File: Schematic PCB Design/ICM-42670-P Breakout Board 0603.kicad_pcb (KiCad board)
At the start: 2 copper layers, 19.5 x 26.5 mm, 14 parts, among them J2 Conn_01x09_Pin, U1 ICM-42670-P, U3 MCP1700x-330xxTT

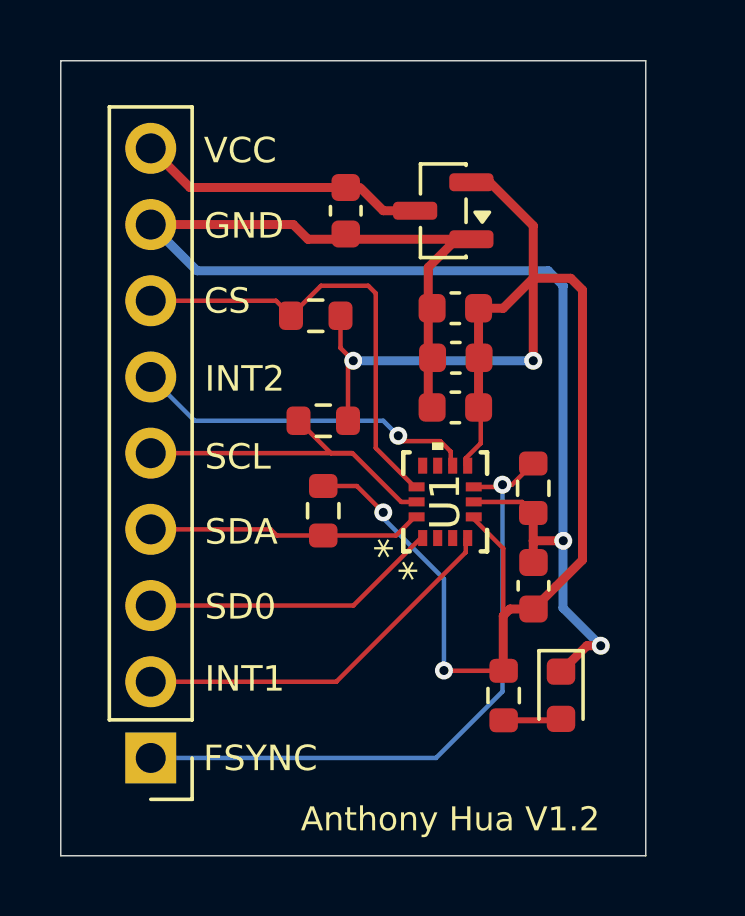
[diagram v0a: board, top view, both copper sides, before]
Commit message: Rerouted Traces and Added Ground Plane
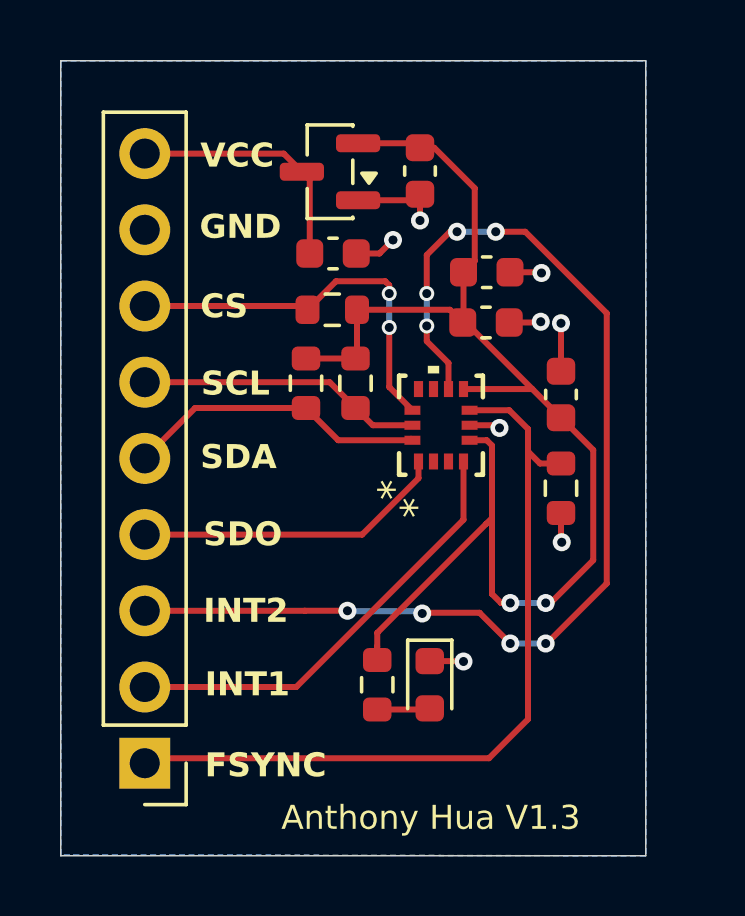
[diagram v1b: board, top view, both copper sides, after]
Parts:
- moved C3 6.44 mm to (72.2, 34.1)
- moved C4 4.72 mm to (67.5, 26.7), turned to 90 degrees
- moved C2 4.63 mm to (69.7, 30.1), turned to 0 degrees
- moved D1 4.39 mm to (67.8, 43.8)
- moved R5 4.29 mm to (63.7, 33.8)
- moved R3 4.23 mm to (66.0, 43.8)
- moved U3 3.99 mm to (64.5, 26.7)
- moved U1 2.56 mm to (68.2, 35.1)
- moved R4 1.65 mm to (65.3, 33.8), turned to 90 degrees
- moved C1 1.55 mm to (69.7, 31.7), turned to 0 degrees
- moved C5 1.49 mm to (64.6, 29.4), turned to 180 degrees
- moved R2 0.92 mm to (72.2, 37.2)
- moved R1 0.59 mm to (64.5, 31.3)
- moved J2 0.27 mm to (58.3, 46.4)
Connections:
- J2 pad 3: /SDO -> /INT2
- J2 pad 4: /SDA -> /SDO
- J2 pad 5: /SCL -> /SDA
- J2 pad 6: /INT2 -> /SCL
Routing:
- net GND: track 50.0 -> 11.0 mm, vias 2 -> 8
- net /INT2: track 11.5 -> 38.0 mm, vias 1 -> 8
- net /3V3_Clean: track 55.7 -> 44.3 mm, vias 4 -> 2
- net /FSYNC: track 22.0 -> 26.5 mm, vias 1 -> 0
- net /CS: track 15.2 -> 13.0 mm, vias 0 -> 2
- net /SCL: track 11.7 -> 9.52 mm
- net /INT1: track 12.8 -> 14.9 mm
- net /SDA: track 9.14 -> 10.1 mm
- net /5V / 3V3: track 9.20 -> 8.32 mm
- net /SDO: track 9.93 -> 10.5 mm
- added copper zone on B.Cu, net GND
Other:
- board text added: "Anthony Hua V1.3"
- board text added: "SDO"
- board text removed: "Anthony Hua V1.2"

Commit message: Add Mounting holes M2
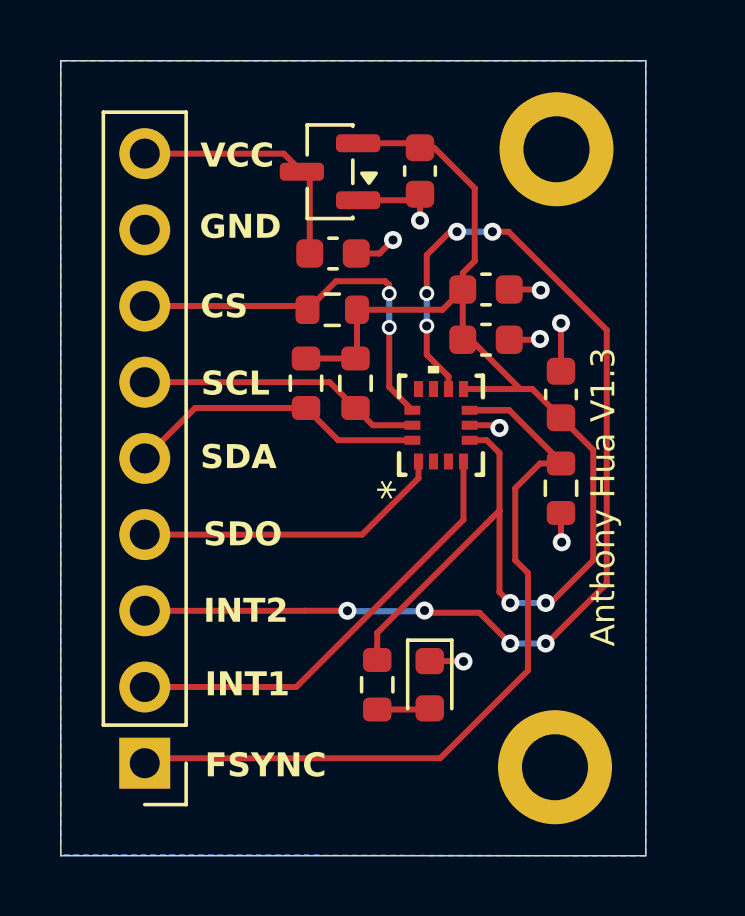
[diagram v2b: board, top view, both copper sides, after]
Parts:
- added REF**: MountingHole_2.2mm_M2_DIN965_Pad, MountingHole:MountingHole_2.2mm_M2_DIN965_Pad, F.Cu at (72.0, 25.9)
- added REF**: MountingHole_2.2mm_M2_DIN965_Pad, MountingHole:MountingHole_2.2mm_M2_DIN965_Pad, F.Cu at (72.0, 46.5)
- moved C2 0.58 mm to (69.7, 30.6)
- moved C1 0.57 mm to (69.7, 32.3)
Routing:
- net /FSYNC: track 26.5 -> 27.3 mm
- net /3V3_Clean: track 44.3 -> 44.8 mm
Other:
- board text added: "ICM-42670"
